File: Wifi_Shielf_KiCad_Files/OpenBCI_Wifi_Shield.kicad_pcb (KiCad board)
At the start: 2 copper layers, 61.2 x 61.2 mm, 32 parts, among them P1 CONN_01X04, P10 CONN_01X04, P2 CONN_01X04, P4 CONN_01X02, P5 CONN_01X02, P6 CONN_01X02, P7 CONN_01X08, P8 CONN_01X08, P9 CONN_01X04, SW1 TACT_SWITCH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

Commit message: Adição dos gerber files e layout da pcb
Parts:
- removed U3: ESP32-WROOM-32, RF_Module:ESP32-WROOM-32
- added IC1: REF200AU, SOIC127P600X175-8N, F.Cu at (115.6, 77.1)
- added IC2: CD4066BE, DIP794W53P254L1930H508Q14N, F.Cu at (100.1, 82.5)
- added J1: Conn_4x1_HDTDCS_Anode(+), Connector_PinHeader_2.54mm:PinHeader_1x05_P2.54mm_Vertical, F.Cu at (103.2, 64.0)
- added J2: Conn_4x1_HDTDCS_Cathode(-), Connector_PinHeader_2.54mm:PinHeader_1x05_P2.54mm_Vertical, F.Cu at (113.4, 69.6)
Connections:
- net Net-(R2-Pad1) renamed /6V
- U1 pad 13: Net-(U1-Pad13) -> /C_C
- U1 pad 19: Net-(U1-Pad19) -> /C_A
- U1 pad 20: Net-(U1-Pad20) -> /C_B
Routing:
- net GND: track 43.3 -> 110.9 mm
- net /6V: track 17.1 -> 71.8 mm, vias 2 -> 5
- net /A_OUT: track 0.00 -> 44.1 mm
- net /I1: track 0.00 -> 38.8 mm, vias 0 -> 2
- net /C_A: track 0.00 -> 30.4 mm, vias 0 -> 1
- net /I2: track 0.00 -> 29.7 mm, vias 0 -> 1
- net /B_OUT: track 0.00 -> 23.6 mm
- net /C_C: track 0.00 -> 22.0 mm
- net /C_B: track 0.00 -> 20.4 mm, vias 0 -> 1
- added copper zone on F.Cu, net GND
- removed copper zone on F.Cu, net +3V3
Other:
- board text added: "OPENTDCS-SHIELD REV v1.0.0"
- board text removed: "OPENBCI-WIFI-SHIELD PTW-OBCI-0001 REV v1.0.0"

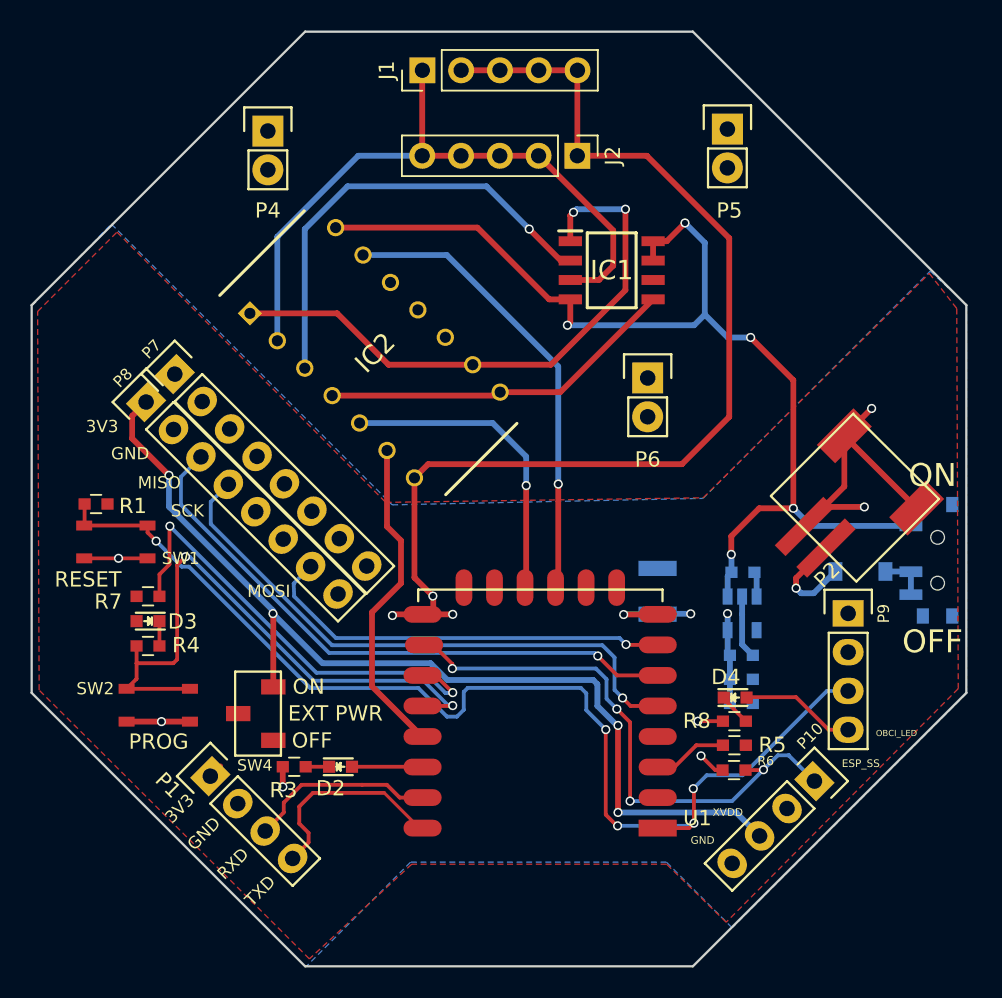
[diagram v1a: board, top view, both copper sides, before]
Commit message: Atualiazação do layout (3.3v conectado)
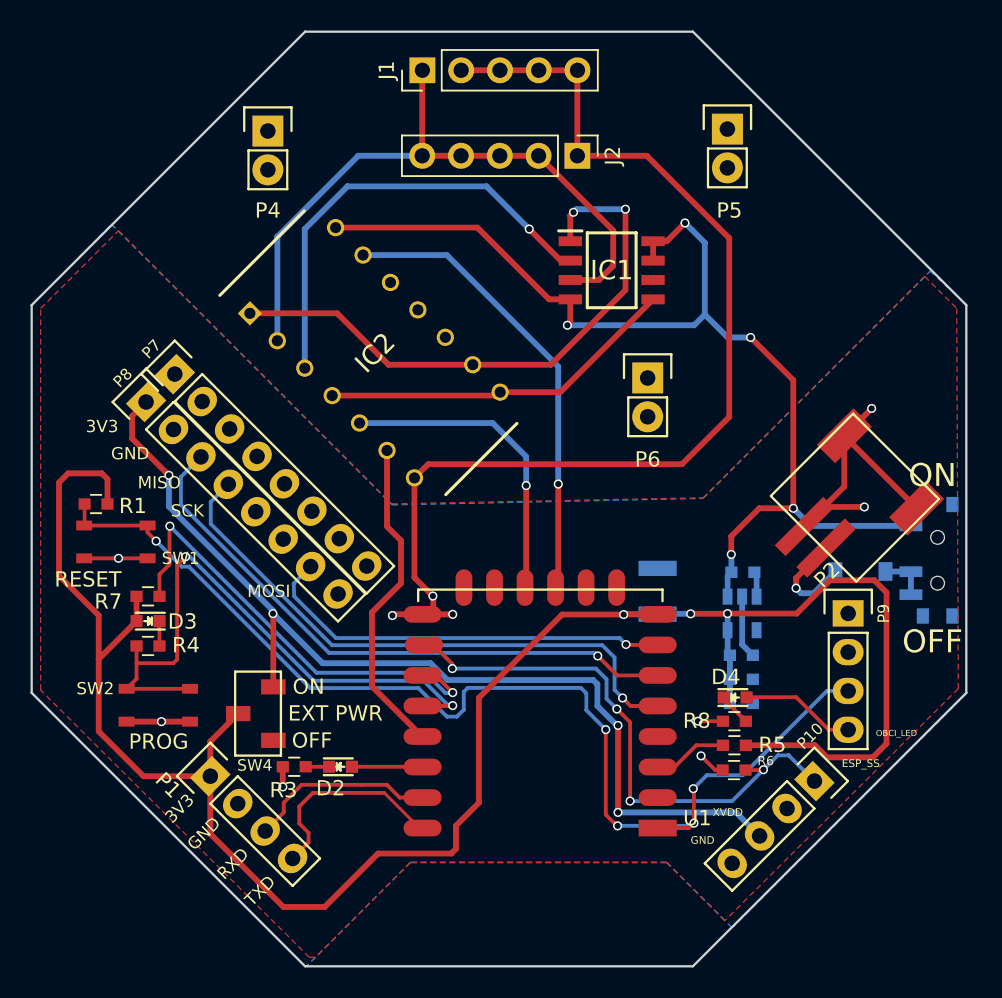
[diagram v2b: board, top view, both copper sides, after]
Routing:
- net +3V3: track 12.9 -> 132.7 mm
